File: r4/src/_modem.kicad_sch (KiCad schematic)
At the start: 53 parts, among them J1 , J11 SMA, J12 U_FL-R-SMT-1_10_, J13 JAE_SIM_Card_SF72S006, J2 , J3 , J4 , J5 , J6 , J7 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

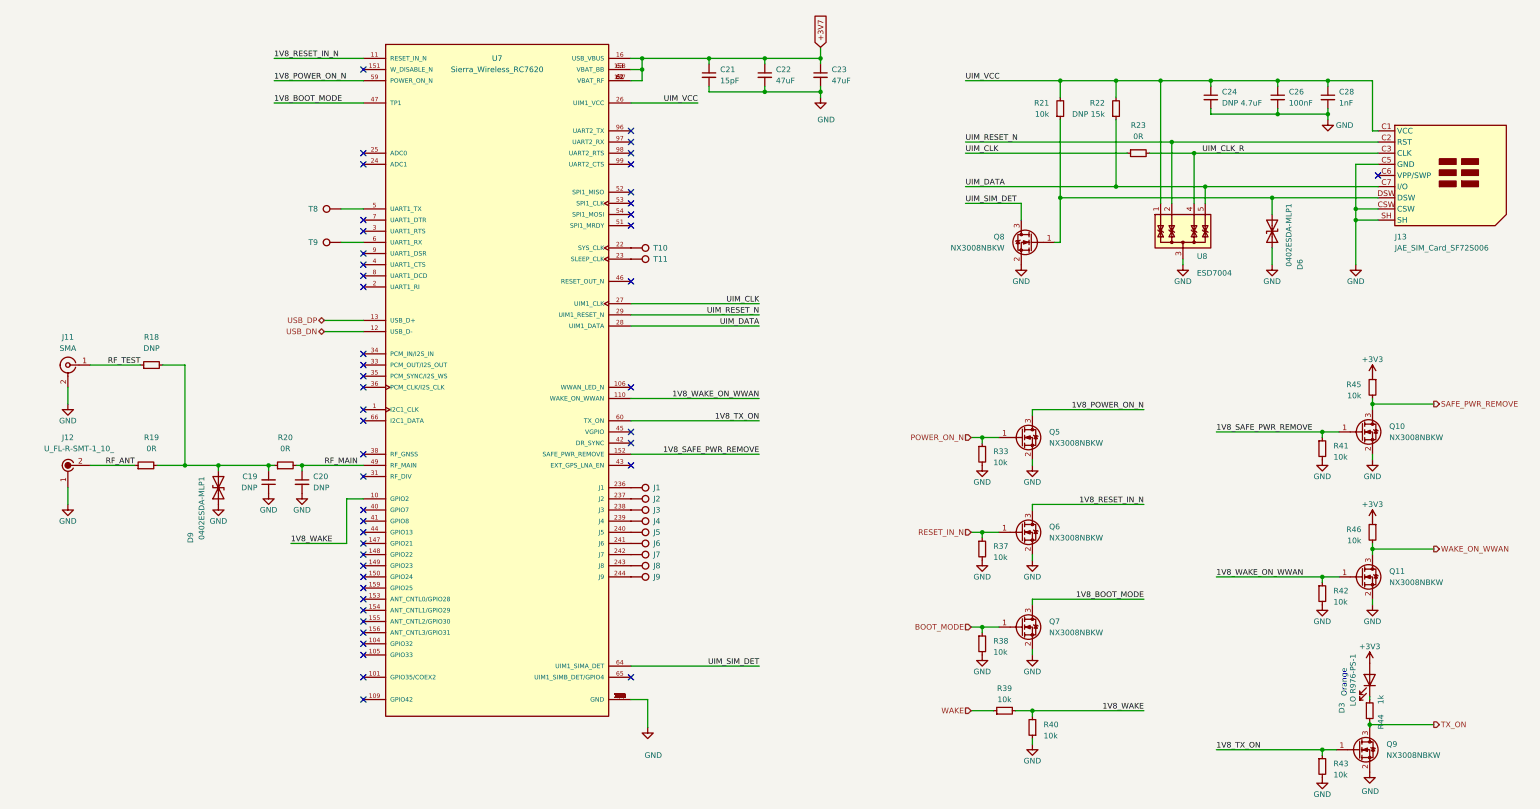
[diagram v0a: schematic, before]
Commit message: Update files to Kicad 6 format
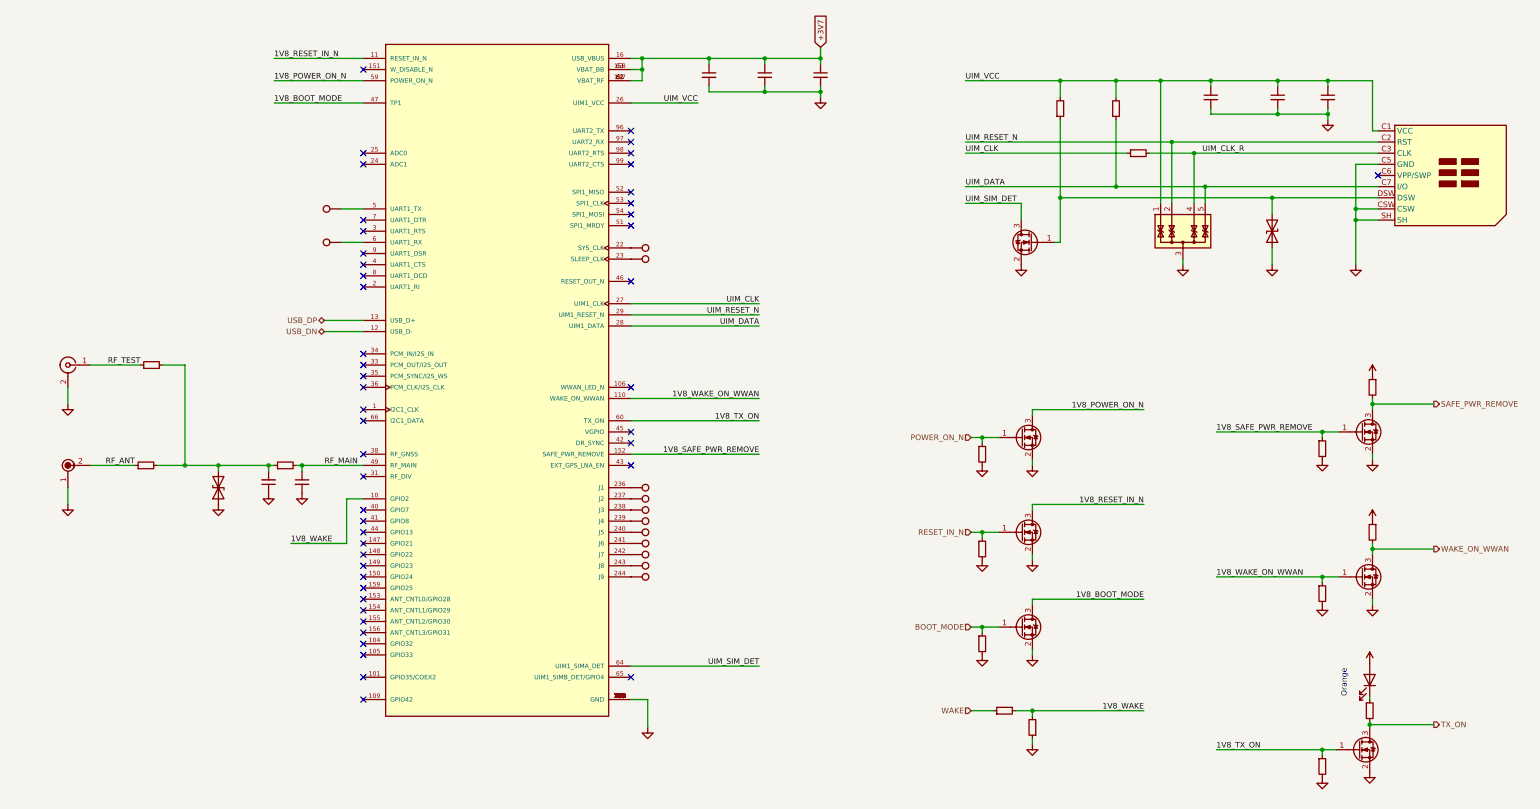
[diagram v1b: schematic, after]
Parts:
- ?: renamed from R46; value 10k -> (none); footprint Resistor_SMD:R_0603_1608Metric -> (none)
- ?: renamed from R38; value 10k -> (none); footprint Resistor_SMD:R_0603_1608Metric -> (none)
- ?: renamed from U7; value Sierra_Wireless_RC7620 -> (none); footprint jeffmakes-footprints:Cellular_Modem-Sierra-Wireless-module-CF3-ringCD -> (none)
- ?: renamed from R42; value 10k -> (none); footprint Resistor_SMD:R_0603_1608Metric -> (none)
- ?: renamed from Q5; value NX3008NBKW -> (none); footprint Package_TO_SOT_SMD:SOT-323_SC-70 -> (none)
- ?: renamed from D6; value 0402ESDA-MLP1 -> (none); footprint Diode_SMD:D_0402_1005Metric -> (none)
- ?: renamed from J2; value (none) -> (none); footprint TestPoint:TestPoint_Pad_D1.0mm -> (none)
- ?: renamed from J6; value (none) -> (none); footprint TestPoint:TestPoint_Pad_D1.0mm -> (none)
- ?: renamed from C23; value 47uF -> (none); footprint Capacitor_SMD:C_0805_2012Metric -> (none)
- ?: renamed from R20; value 0R -> (none); footprint Resistor_SMD:R_0402_1005Metric -> (none)
- ?: renamed from J11; value SMA -> (none); footprint Connector_Coaxial:SMA_Amphenol_132134-10_Vertical -> (none)
- ?: renamed from R19; value 0R -> (none); footprint Resistor_SMD:R_0402_1005Metric -> (none)
- ?: renamed from J5; value (none) -> (none); footprint TestPoint:TestPoint_Pad_D1.0mm -> (none)
- ?: renamed from J4; value (none) -> (none); footprint TestPoint:TestPoint_Pad_D1.0mm -> (none)
- ?: renamed from R37; value 10k -> (none); footprint Resistor_SMD:R_0603_1608Metric -> (none)
- ?: renamed from Q11; value NX3008NBKW -> (none); footprint Package_TO_SOT_SMD:SOT-323_SC-70 -> (none)
- ?: renamed from R41; value 10k -> (none); footprint Resistor_SMD:R_0603_1608Metric -> (none)
- ?: renamed from R23; value 0R -> (none); footprint Resistor_SMD:R_0603_1608Metric -> (none)
- ?: renamed from Q6; value NX3008NBKW -> (none); footprint Package_TO_SOT_SMD:SOT-323_SC-70 -> (none)
- ?: renamed from D9; value 0402ESDA-MLP1 -> (none); footprint Diode_SMD:D_0402_1005Metric -> (none)
- ?: renamed from C19; value DNP -> (none); footprint Capacitor_SMD:C_0402_1005Metric -> (none)
- ?: renamed from D3; value LO R976-PS-1 -> (none); footprint jeffmakes-footprints:CHIPLED-0805 -> (none)
- ?: renamed from J8; value (none) -> (none); footprint TestPoint:TestPoint_Pad_D1.0mm -> (none)
- ?: renamed from C20; value DNP -> (none); footprint Capacitor_SMD:C_0402_1005Metric -> (none)
- ?: renamed from Q10; value NX3008NBKW -> (none); footprint Package_TO_SOT_SMD:SOT-323_SC-70 -> (none)
- ?: renamed from R18; value DNP -> (none); footprint Resistor_SMD:R_0402_1005Metric -> (none)
- ?: renamed from R22; value DNP 15k -> (none); footprint Resistor_SMD:R_0603_1608Metric -> (none)
- ?: renamed from R45; value 10k -> (none); footprint Resistor_SMD:R_0603_1608Metric -> (none)
- ?: renamed from U8; value ESD7004 -> (none); footprint jeffmakes-footprints:USON-10_2.5x1.0mm_P0.5mm -> (none)
- ?: renamed from J12; value U_FL-R-SMT-1_10_ -> (none); footprint digikey-footprints:Coax_Conn_U.FL -> (none)
- ?: renamed from J13; value JAE_SIM_Card_SF72S006 -> (none); footprint Connector_JAE:JAE_SIM_Card_SF72S006 -> (none)
- ?: renamed from R40; value 10k -> (none); footprint Resistor_SMD:R_0603_1608Metric -> (none)
- ?: renamed from C26; value 100nF -> (none); footprint Capacitor_SMD:C_0603_1608Metric -> (none)
- ?: renamed from J1; value (none) -> (none); footprint TestPoint:TestPoint_Pad_D1.0mm -> (none)
- ?: renamed from Q8; value NX3008NBKW -> (none); footprint Package_TO_SOT_SMD:SOT-323_SC-70 -> (none)
- ?: renamed from C21; value 15pF -> (none); footprint Capacitor_SMD:C_0603_1608Metric -> (none)
- ?: renamed from R39; value 10k -> (none); footprint Resistor_SMD:R_0603_1608Metric -> (none)
- ?: renamed from T9; value (none) -> (none); footprint TestPoint:TestPoint_Pad_D1.0mm -> (none)
- ?: renamed from Q9; value NX3008NBKW -> (none); footprint Package_TO_SOT_SMD:SOT-323_SC-70 -> (none)
- ?: renamed from R44; value 1k -> (none); footprint Resistor_SMD:R_0603_1608Metric -> (none)
- ?: renamed from T11; value (none) -> (none); footprint TestPoint:TestPoint_Pad_D1.0mm -> (none)
- ?: renamed from R43; value 10k -> (none); footprint Resistor_SMD:R_0603_1608Metric -> (none)
- ?: renamed from J3; value (none) -> (none); footprint TestPoint:TestPoint_Pad_D1.0mm -> (none)
- ?: renamed from C22; value 47uF -> (none); footprint Capacitor_SMD:C_0805_2012Metric -> (none)
- ?: renamed from R21; value 10k -> (none); footprint Resistor_SMD:R_0603_1608Metric -> (none)
- ?: renamed from T10; value (none) -> (none); footprint TestPoint:TestPoint_Pad_D1.0mm -> (none)
- ?: renamed from T8; value (none) -> (none); footprint TestPoint:TestPoint_Pad_D1.0mm -> (none)
- ?: renamed from J7; value (none) -> (none); footprint TestPoint:TestPoint_Pad_D1.0mm -> (none)
- ?: renamed from J9; value (none) -> (none); footprint TestPoint:TestPoint_Pad_D1.0mm -> (none)
- ?: renamed from R33; value 10k -> (none); footprint Resistor_SMD:R_0603_1608Metric -> (none)
- ?: renamed from C28; value 1nF -> (none); footprint Capacitor_SMD:C_0603_1608Metric -> (none)
- ?: renamed from C24; value DNP 4.7uF -> (none); footprint Capacitor_SMD:C_0805_2012Metric -> (none)
- ?: renamed from Q7; value NX3008NBKW -> (none); footprint Package_TO_SOT_SMD:SOT-323_SC-70 -> (none)
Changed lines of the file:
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@@
-(kicad_sch (version 20210406) (generator eeschema)
+(kicad_sch (version 20220914) (generator eeschema)
   (paper "A3")

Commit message: Remove sole dependency on Digikey library, as they are no longer supported. Only dependency was the U.FL connector and there is an alternative in the native Kicad libs
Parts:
- ?: symbol dk_Coaxial-Connectors-RF:U_FL-R-SMT-1_10_ -> Connector:Conn_Coaxial
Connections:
- net GND: now also ?.2 (Ext); no longer ?.1
- net RF_ANT: now also ?.1 (In); no longer ?.2

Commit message: U.FL connector symbol from Kicad libs
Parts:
- ?: Category Connectors, Interconnects -> (none); DK_Datasheet_Link https://www.hirose.com/product/en/download_file/key_name/U.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 -> (none); DK_Detail_Page /product-detail/en/hirose-electric-co-ltd/U.FL-R-SMT-1(10)/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 -> (none); Digi-Key_PN H11891CT-ND -> (none); Family Coaxial Connectors (RF) -> (none); MPN U.FL-R-SMT-1(10) -> (none); Manufacturer Hirose Electric Co Ltd -> (none)
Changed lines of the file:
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@@
       (effects (font (size 1.27 1.27)) hide)
-    )
-    (property "Digi-Key_PN" "H11891CT-ND" (at 36.83 143.51 0)
-      (effects (font (size 1.524 1.524)) (justify left) hide)
-    )
-    (property "MPN" "U.FL-R-SMT-1(10)" (at 36.83 140.97 0)
-      (effects (font (size 1.524 1.524)) (justify left) hide)
-    )
-    (property "Category" "Connectors, Interconnects" (at 36.83 138.43 0)
-      (effects (font (size 1.524 1.524)) (justify left) hide)
-    )
-    (property "Family" "Coaxial Connectors (RF)" (at 36.83 135.89 0)
-      (effects (font (size 1.524 1.524)) (justify left) hide)
-    )
-    (property "DK_Datasheet_Link" "https://www.hirose.com/product/en/download_file/key_name/U.FL-R-SMT-1%2810%29/category/Drawing%20(2D)/doc_file_id/37627/?file_category_id=6&item_id=03310472210&is_series=U.FL-R-SMT-1(10" (at 36.83 133.35 0)
-      (effects (font (size 1.524 1.524)) (justify left) hide)
-    )
-    (property "DK_Detail_Page" "/product-detail/en/hirose-electric-co-ltd/U.FL-R-SMT-1(10)/H11891CT-ND/2504612" (at 36.83 130.81 0)
-      (effects (font (size 1.524 1.524)) (justify left) hide)
-    )
-    (property "Description" "CONN U.FL RCPT STR 50 OHM SMD" (at 36.83 128.27 0)
-      (effects (font (size 1.524 1.524)) (justify left) hide)
-    )
-    (property "Manufacturer" "Hirose Electric Co Ltd" (at 36.83 125.73 0)
-      (effects (font (size 1.524 1.524)) (justify left) hide)
     )
     (property "Status" "Active" (at 36.83 123.19 0)

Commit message: Delete unnecessary level translator for the deleted SAFE_PWR_REMOVE signal
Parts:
- removed ? (x2): (no value), symbol Device:R_Small
- removed ?: (no value), symbol Device:Q_NMOS_GSD
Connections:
- net 1V8_SAFE_PWR_REMOVE: no longer names the net of ?.152 (SAFE_PWR_REMOVE)
- no-connect marks 48 -> 49
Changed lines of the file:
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@@
   (junction (at 317.5 73.66) (diameter 1.016) (color 0 0 0 0)
   )
-  (junction (at 339.09 139.7) (diameter 1.016) (color 0 0 0 0)
-  )
   (junction (at 335.28 95.25) (diameter 1.016) (color 0 0 0 0)
   )
@@
   )
   (junction (at 326.39 218.44) (diameter 0) (color 0 0 0 0)
-  )
-  (junction (at 327.66 146.05) (diameter 1.016) (color 0 0 0 0)
   )
   (junction (at 328.93 73.66) (diameter 1.016) (color 0 0 0 0)
@@
   (no_connect (at 109.22 140.97))
   (no_connect (at 109.22 143.51))
+  (no_connect (at 170.18 151.13))
   (no_connect (at 340.36 87.63))
-  (wire (pts (xy 170.18 151.13) (xy 199.39 151.13))
-    (stroke (width 0) (type solid))
-  )
   (wire (pts (xy 300.99 90.17) (xy 300.99 93.98))
     (stroke (width 0) (type solid))
@@
     (stroke (width 0) (type solid))
   )
-  (wire (pts (xy 339.09 138.43) (xy 339.09 139.7))
-    (stroke (width 0) (type solid))
-  )
   (wire (pts (xy 246.38 80.01) (xy 293.37 80.01))
     (stroke (width 0) (type solid))
@@
     (stroke (width 0) (type solid))
   )
-  (wire (pts (xy 339.09 152.4) (xy 339.09 151.13))
-    (stroke (width 0) (type solid))
-  )
-  (wire (pts (xy 327.66 146.05) (xy 331.47 146.05))
-    (stroke (width 0) (type solid))
-  )
   (wire (pts (xy 339.09 172.72) (xy 339.09 173.99))
     (stroke (width 0) (type solid))
@@
   )
   (wire (pts (xy 261.62 153.67) (xy 261.62 152.4))
-    (stroke (width 0) (type solid))
-  )
-  (wire (pts (xy 327.66 146.05) (xy 303.53 146.05))
     (stroke (width 0) (type solid))
   )
@@
     (stroke (width 0) (type solid))
   )
-  (wire (pts (xy 353.06 139.7) (xy 339.09 139.7))
-    (stroke (width 0) (type solid))
-  )
   (wire (pts (xy 172.72 60.96) (xy 187.96 60.96))
     (stroke (width 0) (type solid))
@@
     (stroke (width 0) (type solid))
   )
-  (wire (pts (xy 327.66 146.05) (xy 327.66 147.32))
-    (stroke (width 0) (type solid))
-  )
   (wire (pts (xy 326.39 218.44) (xy 326.39 219.71))
     (stroke (width 0) (type solid))
@@
   )
   (wire (pts (xy 170.18 199.39) (xy 199.39 199.39))
-    (stroke (width 0) (type solid))
-  )
-  (wire (pts (xy 339.09 139.7) (xy 339.09 140.97))
     (stroke (width 0) (type solid))
   )
@@
     (effects (font (size 1.27 1.27)) (justify right bottom))
   )
-  (label "1V8_SAFE_PWR_REMOVE" (at 303.53 146.05 0) (fields_autoplaced)
-    (effects (font (size 1.27 1.27)) (justify left bottom))
-  )
   (label "1V8_WAKE_ON_WWAN" (at 303.53 179.07 0) (fields_autoplaced)
     (effects (font (size 1.27 1.27)) (justify left bottom))
@@
   (label "UIM_DATA" (at 246.38 90.17 0) (fields_autoplaced)
     (effects (font (size 1.27 1.27)) (justify left bottom))
-  )
-  (label "1V8_SAFE_PWR_REMOVE" (at 199.39 151.13 180) (fields_autoplaced)
-    (effects (font (size 1.27 1.27)) (justify right bottom))
   )
   (global_label "+3V7" (shape input) (at 213.36 58.42 90)
@@
   (hierarchical_label "WAKE" (shape input) (at 247.65 209.55 180) (fields_autoplaced)
     (effects (font (size 1.27 1.27)) (justify right))
-  )
-  (hierarchical_label "SAFE_PWR_REMOVE" (shape output) (at 353.06 139.7 0) (fields_autoplaced)
-    (effects (font (size 1.27 1.27)) (justify left))
   )
   (hierarchical_label "POWER_ON_N" (shape input) (at 247.65 147.32 180) (fields_autoplaced)
@@
     (pin "3")
   )
-  (symbol (lib_id "Device:R_Small") (at 327.66 149.86 0) (unit 1)
-    (in_bom yes) (on_board yes) (dnp no) (fields_autoplaced)
-    (default_instance (reference "") (unit 1) (value "") (footprint ""))
-    (property "Reference" "" (at 330.2 149.2249 0)
-      (effects (font (size 1.27 1.27)) (justify left))
-    )
-    (property "Value" "" (at 330.2 151.7649 0)
-      (effects (font (size 1.27 1.27)) (justify left))
-    )
-    (property "Footprint" "" (at 327.66 149.86 0)
-      (effects (font (size 1.27 1.27)) hide)
-    )
-    (property "Datasheet" "~" (at 327.66 149.86 0)
-      (effects (font (size 1.27 1.27)) hide)
-    )
-    (pin "1")
-    (pin "2")
-  )
   (symbol (lib_id "Device:R_Small") (at 285.75 82.55 90) (mirror x) (unit 1)
     (in_bom yes) (on_board yes) (dnp no)
@@
     (pin "2")
   )
-  (symbol (lib_id "Device:Q_NMOS_GSD") (at 336.55 146.05 0) (unit 1)
-    (in_bom yes) (on_board yes) (dnp no)
-    (default_instance (reference "") (unit 1) (value "") (footprint ""))
-    (property "Reference" "" (at 342.9 144.78 0)
-      (effects (font (size 1.27 1.27)) (justify left))
-    )
-    (property "Value" "" (at 342.9 147.32 0)
-      (effects (font (size 1.27 1.27)) (justify left))
-    )
-    (property "Footprint" "" (at 341.63 143.51 0)
-      (effects (font (size 1.27 1.27)) hide)
-    )
-    (property "Datasheet" "~" (at 336.55 146.05 0)
-      (effects (font (size 1.27 1.27)) hide)
-    )
-    (pin "1")
-    (pin "2")
-    (pin "3")
-  )
   (symbol (lib_id "Device:R_Small") (at 60.96 130.81 90) (unit 1)
     (in_bom yes) (on_board yes) (dnp no)
@@
     (pin "1")
   )
-  (symbol (lib_id "Device:R_Small") (at 339.09 135.89 0) (mirror y) (unit 1)
-    (in_bom yes) (on_board yes) (dnp no) (fields_autoplaced)
-    (default_instance (reference "") (unit 1) (value "") (footprint ""))
-    (property "Reference" "" (at 336.55 135.2549 0)
-      (effects (font (size 1.27 1.27)) (justify left))
-    )
-    (property "Value" "" (at 336.55 137.7949 0)
-      (effects (font (size 1.27 1.27)) (justify left))
-    )
-    (property "Footprint" "" (at 339.09 135.89 0)
-      (effects (font (size 1.27 1.27)) hide)
-    )
-    (property "Datasheet" "~" (at 339.09 135.89 0)
-      (effects (font (size 1.27 1.27)) hide)
-    )
-    (pin "1")
-    (pin "2")
-  )
   (symbol (lib_id "power:GND") (at 335.28 107.95 0) (unit 1)
     (in_bom yes) (on_board yes) (dnp no)
@@
     )
     (property "Datasheet" "" (at 213.36 69.85 0)
-      (effects (font (size 1.27 1.27)) hide)
-    )
-    (pin "1")
-  )
-  (symbol (lib_id "power:GND") (at 339.09 152.4 0) (unit 1)
-    (in_bom yes) (on_board yes) (dnp no)
-    (default_instance (reference "") (unit 1) (value "") (footprint ""))
-    (property "Reference" "" (at 339.09 158.75 0)
-      (effects (font (size 1.27 1.27)) hide)
-    )
-    (property "Value" "" (at 339.09 156.21 0)
-      (effects (font (size 1.27 1.27)))
-    )
-    (property "Footprint" "" (at 339.09 152.4 0)
-      (effects (font (size 1.27 1.27)) hide)
-    )
-    (property "Datasheet" "" (at 339.09 152.4 0)
       (effects (font (size 1.27 1.27)) hide)
     )
@@
     (pin "4")
     (pin "5")
-  )
-  (symbol (lib_id "power:+3V3") (at 339.09 133.35 0) (mirror y) (unit 1)
-    (in_bom yes) (on_board yes) (dnp no) (fields_autoplaced)
-    (default_instance (reference "") (unit 1) (value "") (footprint ""))
-    (property "Reference" "" (at 339.09 137.16 0)
-      (effects (font (size 1.27 1.27)) hide)
-    )
-    (property "Value" "" (at 339.09 129.54 0)
-      (effects (font (size 1.27 1.27)))
-    )
-    (property "Footprint" "" (at 339.09 133.35 0)
-      (effects (font (size 1.27 1.27)) hide)
-    )
-    (property "Datasheet" "" (at 339.09 133.35 0)
-      (effects (font (size 1.27 1.27)) hide)
-    )
-    (pin "1")
   )
   (symbol (lib_id "Connector:Conn_Coaxial") (at 41.91 153.67 0) (mirror y) (unit 1)
@@
     (pin "2")
   )
-  (symbol (lib_id "power:GND") (at 327.66 152.4 0) (unit 1)
-    (in_bom yes) (on_board yes) (dnp no)
-    (default_instance (reference "") (unit 1) (value "") (footprint ""))
-    (property "Reference" "" (at 327.66 158.75 0)
-      (effects (font (size 1.27 1.27)) hide)
-    )
-    (property "Value" "" (at 327.66 156.21 0)
-      (effects (font (size 1.27 1.27)))
-    )
-    (property "Footprint" "" (at 327.66 152.4 0)
-      (effects (font (size 1.27 1.27)) hide)
-    )
-    (property "Datasheet" "" (at 327.66 152.4 0)
-      (effects (font (size 1.27 1.27)) hide)
-    )
-    (pin "1")
-  )
   (symbol (lib_id "Device:C_Small") (at 302.26 69.85 0) (unit 1)
